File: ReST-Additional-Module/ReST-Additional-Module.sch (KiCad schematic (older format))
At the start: 8 parts, among them P1 CONN_02X09, P2 CONN_01X08, P3 CONN_02X08, P4 CONN_01X02, P5 CONN_01X02, P6 CONN_01X02, P7 CONN_01X02, U1 ULN2803

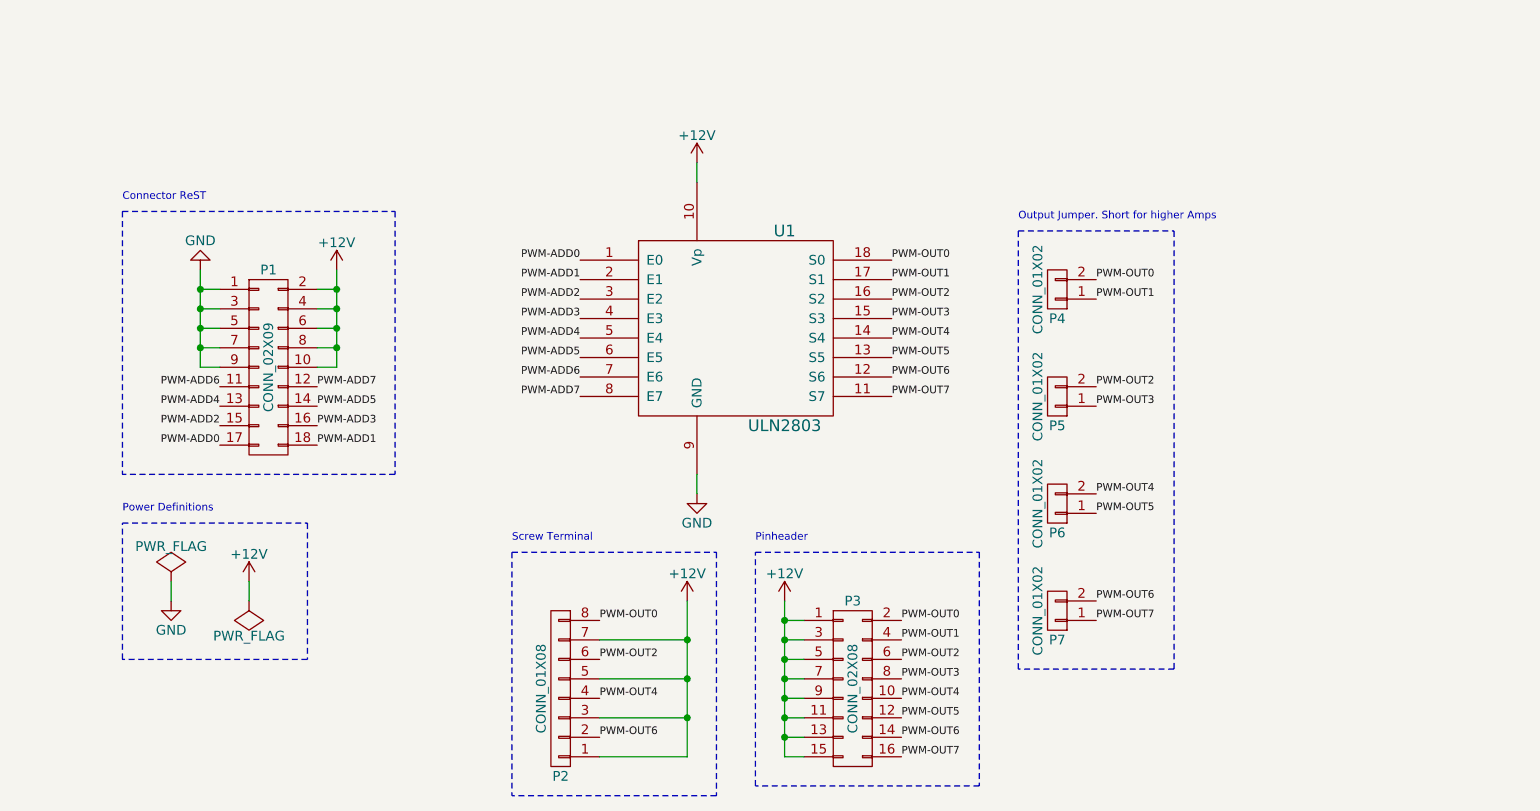
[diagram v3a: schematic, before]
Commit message: Changed ADD Board to use less Pins
Now only 4 Channels, but everyone ~0.6A capable
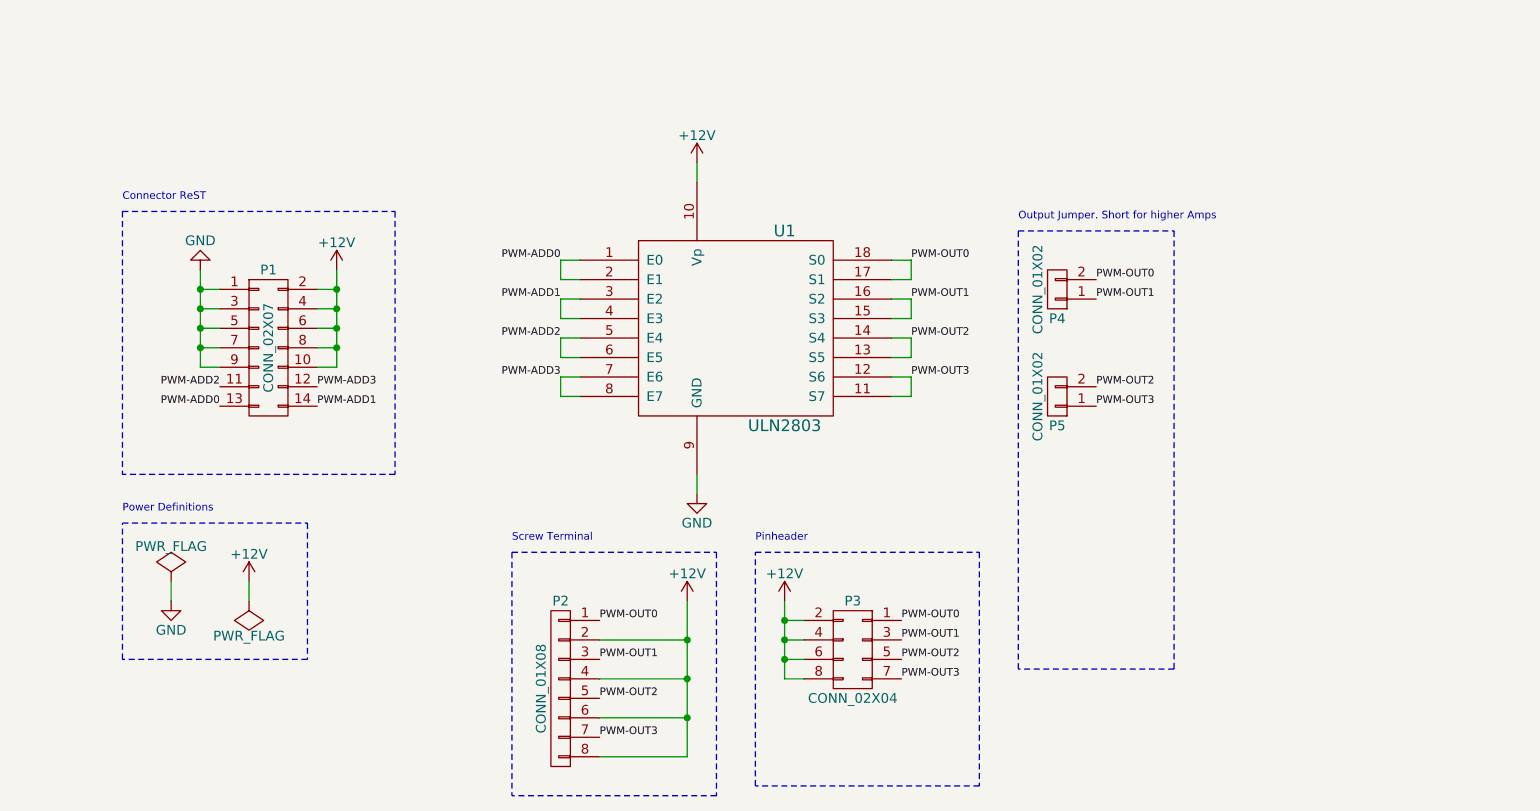
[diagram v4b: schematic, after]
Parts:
- removed P1: CONN_02X09, Pin_Headers:Pin_Header_Angled_2x09, symbol CONN_02X09
- removed P3: CONN_02X08, Pin_Headers:Pin_Header_Straight_2x08, symbol CONN_02X08
- removed P6, P7: CONN_01X02, Pin_Headers:Pin_Header_Straight_1x02, symbol CONN_01X02
- added P1: CONN_02X07, Pin_Headers:Pin_Header_Angled_2x07, symbol CONN_02X07
- added P3: CONN_02X04, Pin_Headers:Pin_Header_Straight_2x04, symbol CONN_02X04
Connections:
- net PWM-ADD4 is gone; now on net PWM-ADD2: U1.5 (E4)
- net PWM-ADD5 is gone; now on net PWM-ADD2: U1.6 (E5)
- net PWM-ADD6 is gone; now on net PWM-ADD3: U1.7 (E6)
- net PWM-ADD7 is gone; now on net PWM-ADD3: U1.8 (E7)
- net PWM-OUT5 is gone; now on net PWM-OUT2: U1.13 (S5)
- net PWM-OUT7 is gone; now on net PWM-OUT3: U1.11 (S7)
- net +12V: now also P2.2 (P2), P2.4 (P4), P2.6 (P6), P2.8 (P8), P1.10 (P10), P1.2 (P2), P1.4 (P4), P1.6 (P6), P1.8 (P8), P3.2 (P2), P3.4 (P4), P3.6 (P6), P3.8 (P8); no longer P2.1 (P1), P2.3 (P3), P2.5 (P5), P2.7 (P7)
- net GND: now also P1.1 (P1), P1.3 (P3), P1.5 (P5), P1.7 (P7), P1.9 (P9)
- net PWM-ADD0: now also U1.2 (E1), P1.13 (P13)
- net PWM-ADD1: now also U1.3 (E2), U1.4 (E3), P1.14 (P14); no longer U1.2 (E1)
- net PWM-ADD2: now also P1.11 (P11); no longer U1.3 (E2)
- net PWM-ADD3: now also P1.12 (P12); no longer U1.4 (E3)
- net PWM-OUT0: now also P2.1 (P1), U1.17 (S1), P3.1 (P1); no longer P2.8 (P8)
- net PWM-OUT1: now also P2.3 (P3), U1.15 (S3), U1.16 (S2), P3.3 (P3); no longer U1.17 (S1)
- net PWM-OUT2: now also P2.5 (P5), U1.14 (S4), P3.5 (P5); no longer P2.6 (P6), U1.16 (S2)
- net PWM-OUT3: now also P2.7 (P7), U1.12 (S6), P3.7 (P7); no longer U1.15 (S3)
- removed net PWM-OUT4: P2.4 (P4), U1.14 (S4)
- removed net PWM-OUT6: P2.2 (P2), U1.12 (S6)
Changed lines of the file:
@@
 	-1   0    0    1
 $EndComp
-$Comp
-L CONN_02X09 P1
-U 1 1 56B9E993
-P 3950 3150
-F 0 "P1" H 3950 3650 50  0000 C CNN
-F 1 "CONN_02X09" V 3950 3150 50  0000 C CNN
-F 2 "Pin_Headers:Pin_Header_Angled_2x09" H 3950 1950 39  0001 C CNN
-F 3 "" H 3950 1950 50  0000 C CNN
-	1    3950 3150
-	1    0    0    -1
-$EndComp
-Text Label 3700 3550 2    39   ~ 0
+Text Label 3700 3350 2    39   ~ 0
 PWM-ADD0
-Text Label 3700 3450 2    39   ~ 0
+Text Label 3700 3250 2    39   ~ 0
 PWM-ADD2
-Text Label 3700 3350 2    39   ~ 0
-PWM-ADD4
-Text Label 3700 3250 2    39   ~ 0
-PWM-ADD6
 Text Label 4200 3250 0    39   ~ 0
-PWM-ADD7
+PWM-ADD3
 Text Label 4200 3350 0    39   ~ 0
-PWM-ADD5
-Text Label 4200 3450 0    39   ~ 0
-PWM-ADD3
-Text Label 4200 3550 0    39   ~ 0
 PWM-ADD1
 $Comp
@@
 	1    0    0    -1
 $EndComp
-Text Label 5550 2600 2    39   ~ 0
+Text Label 5450 2600 2    39   ~ 0
 PWM-ADD0
-Text Label 5550 2800 2    39   ~ 0
+Text Label 5450 3000 2    39   ~ 0
 PWM-ADD2
-Text Label 5550 3000 2    39   ~ 0
-PWM-ADD4
-Text Label 5550 3200 2    39   ~ 0
-PWM-ADD6
-Text Label 5550 2700 2    39   ~ 0
+Text Label 5450 2800 2    39   ~ 0
 PWM-ADD1
-Text Label 5550 2900 2    39   ~ 0
+Text Label 5450 3200 2    39   ~ 0
 PWM-ADD3
-Text Label 5550 3100 2    39   ~ 0
-PWM-ADD5
-Text Label 5550 3300 2    39   ~ 0
-PWM-ADD7
 $Comp
 L CONN_01X08 P2
@@
 F 3 "" H 5450 4800 50  0000 C CNN
 	1    5450 4800
-	-1   0    0    1
-$EndComp
-$Comp
-L CONN_02X08 P3
-U 1 1 56B9EDEC
-P 6950 4800
-F 0 "P3" H 6950 5250 50  0000 C CNN
-F 1 "CONN_02X08" V 6950 4800 50  0000 C CNN
-F 2 "Pin_Headers:Pin_Header_Straight_2x08" H 6950 3600 50  0001 C CNN
-F 3 "" H 6950 3600 50  0000 C CNN
-	1    6950 4800
-	1    0    0    -1
-$EndComp
-Text Label 7150 2600 0    39   ~ 0
+	-1   0    0    -1
+$EndComp
+Text Label 7250 2600 0    39   ~ 0
 PWM-OUT0
-Text Label 7150 2700 0    39   ~ 0
+Text Label 7250 2800 0    39   ~ 0
 PWM-OUT1
-Text Label 7150 2800 0    39   ~ 0
+Text Label 7250 3000 0    39   ~ 0
 PWM-OUT2
-Text Label 7150 2900 0    39   ~ 0
+Text Label 7250 3200 0    39   ~ 0
 PWM-OUT3
-Text Label 7150 3000 0    39   ~ 0
-PWM-OUT4
-Text Label 7150 3100 0    39   ~ 0
-PWM-OUT5
-Text Label 7150 3200 0    39   ~ 0
-PWM-OUT6
-Text Label 7150 3300 0    39   ~ 0
-PWM-OUT7
 Text Label 7200 4450 0    39   ~ 0
 PWM-OUT0
@@
 Text Label 7200 4750 0    39   ~ 0
 PWM-OUT3
-Text Label 7200 4850 0    39   ~ 0
-PWM-OUT4
-Text Label 7200 4950 0    39   ~ 0
-PWM-OUT5
-Text Label 7200 5050 0    39   ~ 0
-PWM-OUT6
-Text Label 7200 5150 0    39   ~ 0
-PWM-OUT7
 $Comp
 L +12V #PWR07
@@
 PWM-OUT0
 Text Label 5650 4650 0    39   ~ 0
+PWM-OUT1
+Text Label 5650 4850 0    39   ~ 0
 PWM-OUT2
-Text Label 5650 4850 0    39   ~ 0
-PWM-OUT4
 Text Label 5650 5050 0    39   ~ 0
-PWM-OUT6
+PWM-OUT3
 $Comp
 L +12V #PWR08
@@
 	-1   0    0    1
 $EndComp
-$Comp
-L CONN_01X02 P6
-U 1 1 56B9F6DD
-P 8000 3850
-F 0 "P6" H 8000 4000 50  0000 C CNN
-F 1 "CONN_01X02" V 8100 3850 50  0000 C CNN
-F 2 "Pin_Headers:Pin_Header_Straight_1x02" H 8000 3850 50  0001 C CNN
-F 3 "" H 8000 3850 50  0000 C CNN
-	1    8000 3850
-	-1   0    0    1
-$EndComp
-$Comp
-L CONN_01X02 P7
-U 1 1 56B9F745
-P 8000 4400
-F 0 "P7" H 8000 4550 50  0000 C CNN
-F 1 "CONN_01X02" V 8100 4400 50  0000 C CNN
-F 2 "Pin_Headers:Pin_Header_Straight_1x02" H 8000 4400 50  0001 C CNN
-F 3 "" H 8000 4400 50  0000 C CNN
-	1    8000 4400
-	-1   0    0    1
-$EndComp
 Text Label 8200 3250 0    39   ~ 0
 PWM-OUT2
 Text Label 8200 3350 0    39   ~ 0
 PWM-OUT3
-Text Label 8200 3800 0    39   ~ 0
-PWM-OUT4
-Text Label 8200 3900 0    39   ~ 0
-PWM-OUT5
-Text Label 8200 4350 0    39   ~ 0
-PWM-OUT6
-Text Label 8200 4450 0    39   ~ 0
-PWM-OUT7
 $Comp
 L GND #PWR09
@@
 	6700 4450 6600 4450
 Wire Wire Line
-	6600 4350 6600 5150
-Wire Wire Line
-	6600 5150 6700 5150
+	6600 4350 6600 4750
 Connection ~ 6600 4450
 Wire Wire Line
@@
 Wire Wire Line
 	6600 4750 6700 4750
-Connection ~ 6600 4750
-Wire Wire Line
-	6700 4850 6600 4850
-Connection ~ 6600 4850
-Wire Wire Line
-	6700 4950 6600 4950
-Connection ~ 6600 4950
-Wire Wire Line
-	6600 5050 6700 5050
-Connection ~ 6600 5050
 Wire Wire Line
 	6100 5150 5650 5150
@@
 Text Notes 5200 4050 0    39   ~ 0
 Screw Terminal
+$Comp
+L CONN_02X07 P1
+U 1 1 56C9A3DE
+P 3950 3050
+F 0 "P1" H 3950 3450 50  0000 C CNN
+F 1 "CONN_02X07" V 3950 3050 50  0000 C CNN
+F 2 "Pin_Headers:Pin_Header_Angled_2x07" H 3950 1850 50  0001 C CNN
+F 3 "" H 3950 1850 50  0000 C CNN
+	1    3950 3050
+	1    0    0    -1
+$EndComp
+Wire Wire Line
+	5450 2600 5550 2600
+Wire Wire Line
+	5450 2600 5450 2700
+Wire Wire Line
+	5450 2700 5550 2700
+Wire Wire Line
+	5450 2800 5550 2800
+Wire Wire Line
+	5450 2800 5450 2900
+Wire Wire Line
+	5450 2900 5550 2900
+Wire Wire Line
+	5450 3000 5550 3000
+Wire Wire Line
+	5450 3000 5450 3100
+Wire Wire Line
+	5450 3100 5550 3100
+Wire Wire Line
+	5450 3200 5550 3200
+Wire Wire Line
+	5450 3200 5450 3300
+Wire Wire Line
+	5450 3300 5550 3300
+Wire Wire Line
+	7250 2600 7150 2600
+Wire Wire Line
+	7150 2700 7250 2700
+Wire Wire Line
+	7250 2700 7250 2600
+Wire Wire Line
+	7250 2800 7250 2900
+Wire Wire Line
+	7250 2900 7150 2900
+Wire Wire Line
+	7250 2800 7150 2800
+Wire Wire Line
+	7250 3000 7250 3100
+Wire Wire Line
+	7250 3100 7150 3100
+Wire Wire Line
+	7250 3000 7150 3000
+Wire Wire Line
+	7250 3200 7150 3200
+Wire Wire Line
+	7250 3200 7250 3300
+Wire Wire Line
+	7250 3300 7150 3300
+$Comp
+L CONN_02X04 P3
+U 1 1 56C9B25D
+P 6950 4600
+F 0 "P3" H 6950 4850 50  0000 C CNN
+F 1 "CONN_02X04" H 6950 4350 50  0000 C CNN
+F 2 "Pin_Headers:Pin_Header_Straight_2x04" H 6950 3400 50  0001 C CNN
+F 3 "" H 6950 3400 50  0000 C CNN
+	1    6950 4600
+	-1   0    0    -1
+$EndComp
 $EndSCHEMATC

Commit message: Added Images and PDF's
+ Silkscreening
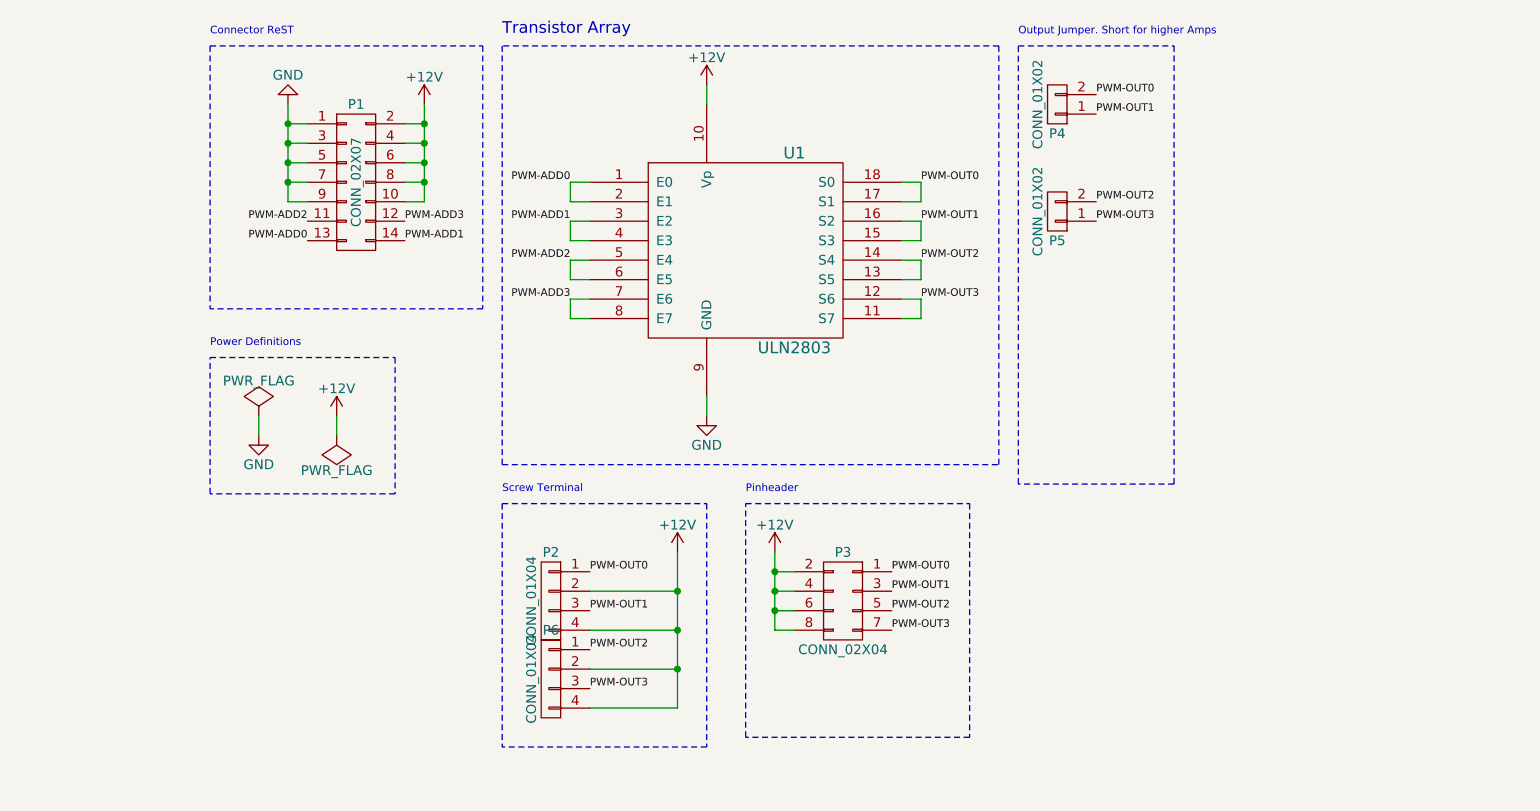
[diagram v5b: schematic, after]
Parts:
- removed P2: CONN_01X08, 2:mpt_0,5%2f8-2,54, symbol CONN_01X08
- added P2, P6: CONN_01X04, ReST-Library:screw-2,54-4P, symbol CONN_01X04
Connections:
- net +12V: now also P2.2 (P2), P2.4 (P4), P6.2 (P2), P6.4 (P4)
- net PWM-OUT0: now also P2.1 (P1)
- net PWM-OUT1: now also P2.3 (P3)
- net PWM-OUT2: now also P6.1 (P1)
- net PWM-OUT3: now also P6.3 (P3)
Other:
- note added: "Transistor Array"
- moved on the sheet: P1, P3, P4, P5, U1

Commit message: Removed unnecessary Libs and finished SD Card Module
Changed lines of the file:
@@
 LIBS:Zilog
 LIBS:Dispositivos_I2C
+LIBS:ReST-Library
 LIBS:ReST-Additional-Module-cache
 EELAYER 25 0
@@
 Text Label 4650 2500 0    39   ~ 0
 PWM-ADD1
-$Comp
-L ULN2803 U1
-U 1 1 56B9EB55
-P 6400 2550
-F 0 "U1" H 6650 3050 60  0000 C CNN
-F 1 "ULN2803" H 6650 2050 60  0000 C CNN
-F 2 "Housings_DIP:DIP-18_W7.62mm_LongPads" H 6400 2550 39  0001 C CNN
-F 3 "" H 6400 2550 39  0000 C CNN
-	1    6400 2550
-	1    0    0    -1
-$EndComp
 Text Label 5500 2200 2    39   ~ 0
 PWM-ADD0
@@
 	3650 3800 3650 3100
 Wire Wire Line
-	4750 1800 4750 2300
+	4750 1800 4750 1900
+Wire Wire Line
+	4750 1900 4750 2000
+Wire Wire Line
+	4750 2000 4750 2100
+Wire Wire Line
+	4750 2100 4750 2200
+Wire Wire Line
+	4750 2200 4750 2300
 Wire Wire Line
 	4750 1900 4650 1900
@@
 Connection ~ 4750 2100
 Wire Wire Line
-	4050 1800 4050 2300
+	4050 1800 4050 1900
+Wire Wire Line
+	4050 1900 4050 2000
+Wire Wire Line
+	4050 2000 4050 2100
+Wire Wire Line
+	4050 2100 4050 2200
+Wire Wire Line
+	4050 2200 4050 2300
 Wire Wire Line
 	4050 1900 4150 1900
@@
 	6650 4200 6550 4200
 Wire Wire Line
-	6550 4100 6550 4500
+	6550 4100 6550 4200
+Wire Wire Line
+	6550 4200 6550 4300
+Wire Wire Line
+	6550 4300 6550 4400
+Wire Wire Line
+	6550 4400 6550 4500
 Connection ~ 6550 4200
 Wire Wire Line
@@
 	6050 4900 5600 4900
 Wire Wire Line
-	6050 4100 6050 4900
+	6050 4100 6050 4300
+Wire Wire Line
+	6050 4300 6050 4500
+Wire Wire Line
+	6050 4500 6050 4700
+Wire Wire Line
+	6050 4700 6050 4900
 Wire Wire Line
 	5600 4700 6050 4700
@@
 	-1   0    0    -1
 $EndComp
+$Comp
+L ULN2803 U1
+U 1 1 56D4E527
+P 6400 2550
+F 0 "U1" H 6650 3050 60  0000 C CNN
+F 1 "ULN2803" H 6650 2050 60  0000 C CNN
+F 2 "Housings_DIP:DIP-18_W7.62mm_LongPads" H 6400 2550 60  0001 C CNN
+F 3 "" H 6400 2550 60  0000 C CNN
+	1    6400 2550
+	1    0    0    -1
+$EndComp
 $EndSCHEMATC
